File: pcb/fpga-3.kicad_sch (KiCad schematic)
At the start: 6 parts, among them U7 XC7A100T-FGG484, Y1 SiT9365AI-2B2-33E200.000000

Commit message: jtag, dcplng
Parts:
- added C109, C110, C111, C112, C113, C114, C115, C116, C117, C118, C119, C120: 0.1uF, Capacitor_SMD:C_0402_1005Metric, symbol library:C
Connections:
- net 1V35_FD: now also C109.2, C110.2, C111.2, C112.2, C113.2, C114.2, C115.2, C116.2, C117.2, C118.2, C119.2, C120.2
- net GND: now also C109.1, C110.1, C111.1, C112.1, C113.1, C114.1, C115.1, C116.1, C117.1, C118.1, C119.1, C120.1

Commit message: decoupling
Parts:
- removed C109, C110, C111, C112, C113, C114: 0.1uF, Capacitor_SMD:C_0402_1005Metric, symbol library:C
- added C146, C147, C148, C149, C150, C151: 0.1uF, Capacitor_SMD:C_0402_1005Metric, symbol library:C
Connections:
- net GND: now also C146.1, C147.1, C148.1, C149.1, C150.1, C151.1
- net 1V35_FD renamed 1V35_DDR
- net 1V35_DDR: now also C146.2, C147.2, C148.2, C149.2, C150.2, C151.2

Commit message: bom
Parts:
- C42: renamed from C17; Part Description 0.1uF 10% 16V Ceramic Capacitor X7R 0402 (1005 Metric) -> CAP CER 0.1UF 16V X7R 0402
- C43: renamed from C18; Part Description 0.1uF 10% 16V Ceramic Capacitor X7R 0402 (1005 Metric) -> CAP CER 0.1UF 16V X7R 0402
- C44: renamed from C146; Part Description (none) -> CAP CER 0.1UF 16V X7R 0402
- C45: renamed from C115; Part Description (none) -> CAP CER 0.1UF 16V X7R 0402
- C46: renamed from C147; Part Description (none) -> CAP CER 0.1UF 16V X7R 0402
- C47: renamed from C116; Part Description (none) -> CAP CER 0.1UF 16V X7R 0402
- C48: renamed from C148; Part Description (none) -> CAP CER 0.1UF 16V X7R 0402
- C49: renamed from C117; Part Description (none) -> CAP CER 0.1UF 16V X7R 0402
- C50: renamed from C149; Part Description (none) -> CAP CER 0.1UF 16V X7R 0402
- C51: renamed from C118; Part Description (none) -> CAP CER 0.1UF 16V X7R 0402
- C52: renamed from C150; Part Description (none) -> CAP CER 0.1UF 16V X7R 0402
- C53: renamed from C119; Part Description (none) -> CAP CER 0.1UF 16V X7R 0402
- C54: renamed from C151; Part Description (none) -> CAP CER 0.1UF 16V X7R 0402
- C55: renamed from C120; Part Description (none) -> CAP CER 0.1UF 16V X7R 0402
- R23: renamed from R22; Manufacturer (none) -> Vishay Dale; Manufacturer Product Number (none) -> CRCW04024K70FKED; Part Description (none) -> RES 4.7K OHM 1% 1/16W 0402
- R24: renamed from R23; Manufacturer (none) -> Vishay Dale; Manufacturer Product Number (none) -> CRCW04024K70FKED; Part Description (none) -> RES 4.7K OHM 1% 1/16W 0402
- U7: Manufacturer (none) -> AMD; Manufacturer Product Number (none) -> XC7A100T-1FGG484C; Part Description (none) -> IC FPGA 285 I/O 484FBGA
- Y1: Manufacturer (none) -> SiTime; Manufacturer Product Number (none) -> SIT9365AI-2B2-33E200.000000; Part Description (none) -> MEMS OSC XO 200.0000MHZ LVDS SMD

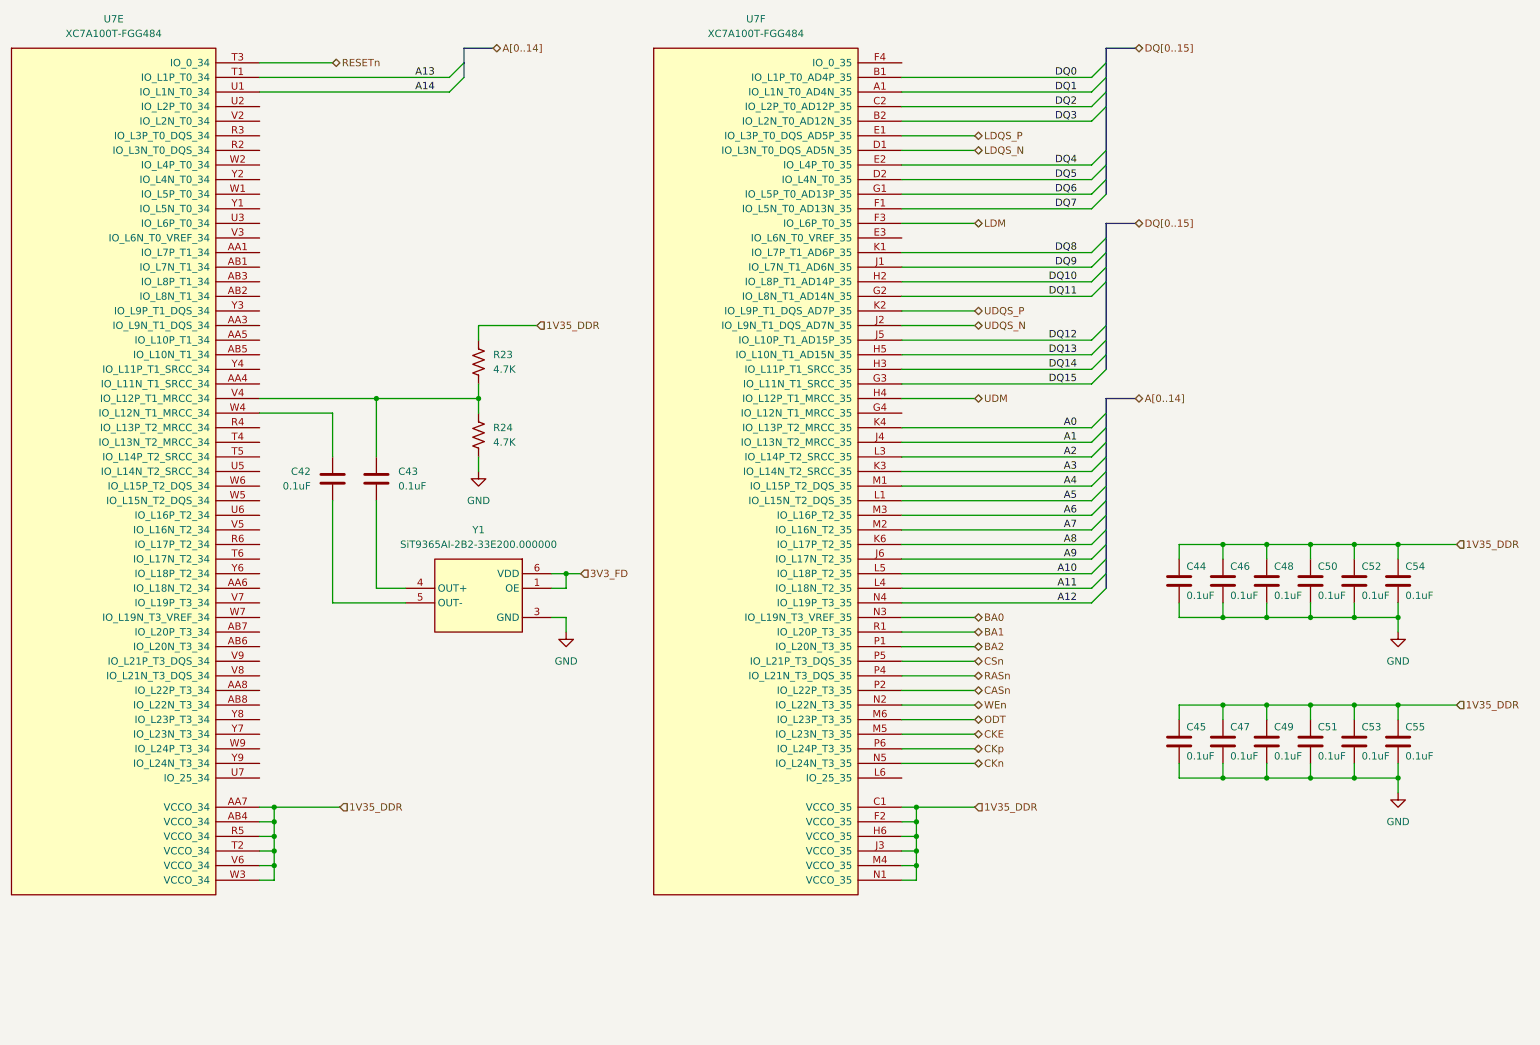
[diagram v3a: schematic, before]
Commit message: added mig ddr pinout constraints
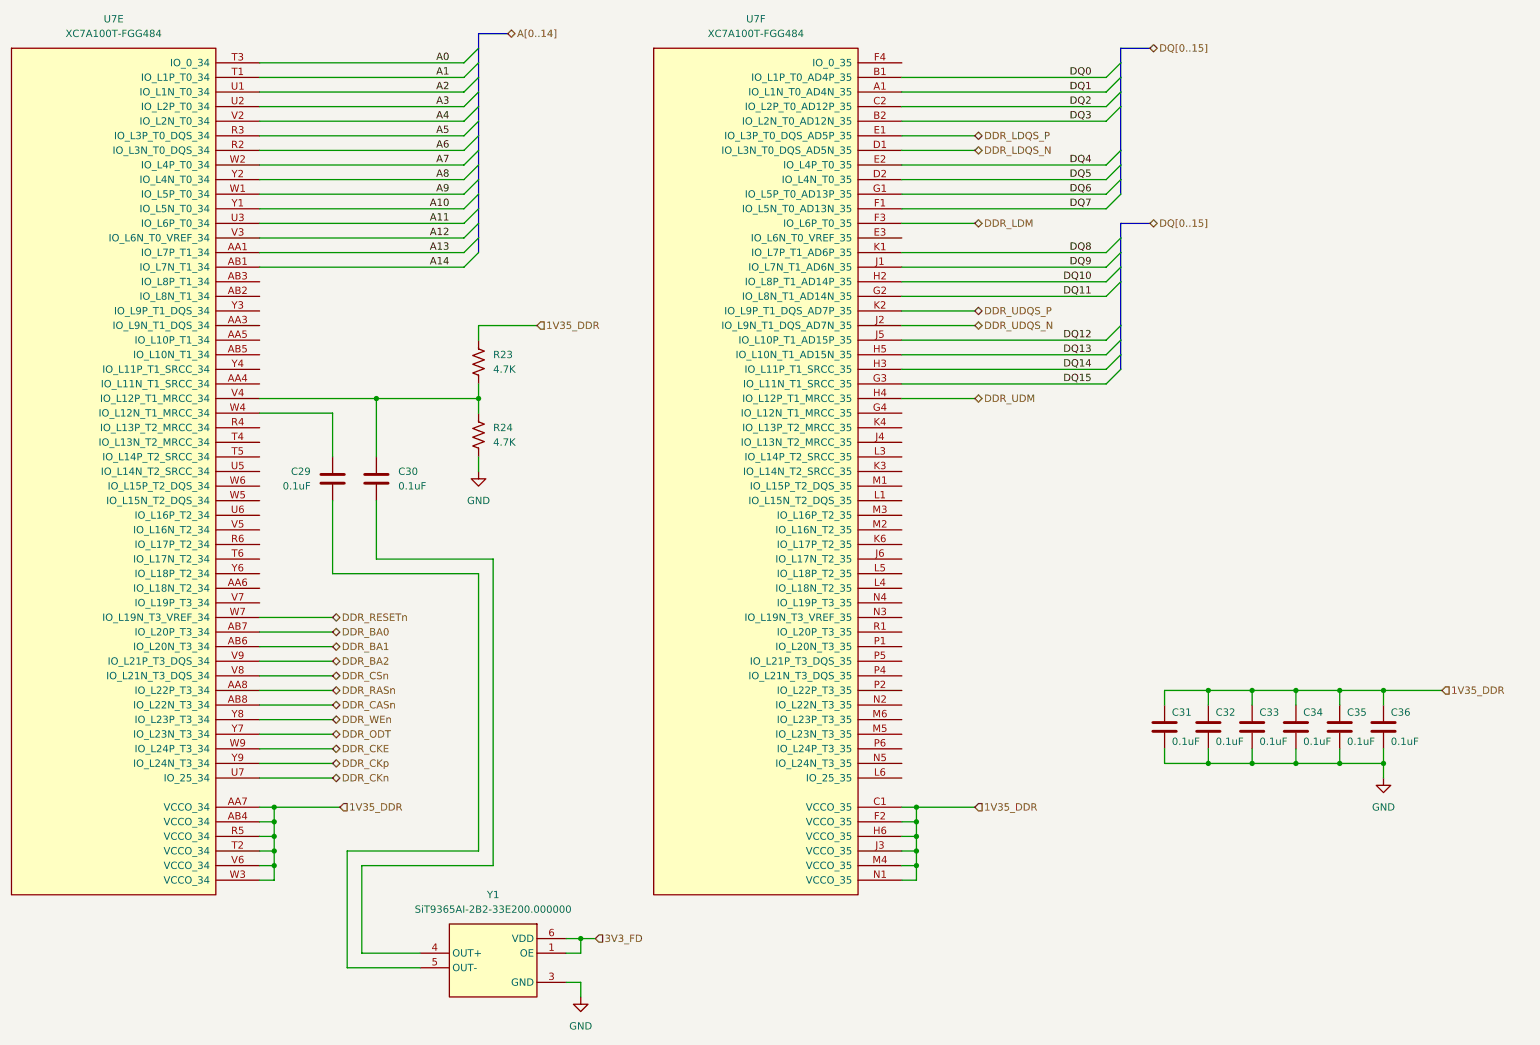
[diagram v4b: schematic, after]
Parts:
- removed C45, C47, C49, C51, C53, C55: 0.1uF, Capacitor_SMD:C_0402_1005Metric, symbol library:C
- renumbered C42 to C29, C43 to C30, C44 to C31, C46 to C32, C48 to C33, C50 to C34, C52 to C35, C54 to C36
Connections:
- net RESETn is gone; now on net A0: U7.T3 (IO_0_34)
- net A0: no longer U7.K4 (IO_L13P_T2_MRCC_35)
- net A1: now also U7.T1 (IO_L1P_T0_34); no longer U7.J4 (IO_L13N_T2_MRCC_35)
- net A10: now also U7.Y1 (IO_L5N_T0_34); no longer U7.L5 (IO_L18P_T2_35)
- net A11: now also U7.U3 (IO_L6P_T0_34); no longer U7.L4 (IO_L18N_T2_35)
- net A12: now also U7.V3 (IO_L6N_T0_VREF_34); no longer U7.N4 (IO_L19P_T3_35)
- net A13: now also U7.AA1 (IO_L7P_T1_34); no longer U7.T1 (IO_L1P_T0_34)
- net A14: now also U7.AB1 (IO_L7N_T1_34); no longer U7.U1 (IO_L1N_T0_34)
- net A2: now also U7.U1 (IO_L1N_T0_34); no longer U7.L3 (IO_L14P_T2_SRCC_35)
- net A3: now also U7.U2 (IO_L2P_T0_34); no longer U7.K3 (IO_L14N_T2_SRCC_35)
- net A4: now also U7.V2 (IO_L2N_T0_34); no longer U7.M1 (IO_L15P_T2_DQS_35)
- net A5: now also U7.R3 (IO_L3P_T0_DQS_34); no longer U7.L1 (IO_L15N_T2_DQS_35)
- net A6: now also U7.R2 (IO_L3N_T0_DQS_34); no longer U7.M3 (IO_L16P_T2_35)
- net A7: now also U7.W2 (IO_L4P_T0_34); no longer U7.M2 (IO_L16N_T2_35)
- net A8: now also U7.Y2 (IO_L4N_T0_34); no longer U7.K6 (IO_L17P_T2_35)
- net A9: now also U7.W1 (IO_L5P_T0_34); no longer U7.J6 (IO_L17N_T2_35)
- net DDR_RASn: now reaches U7.AA8 (IO_L22P_T3_34)
- net DDR_BA1: now reaches U7.AB6 (IO_L20N_T3_34)
- net DDR_BA0: now reaches U7.AB7 (IO_L20P_T3_34)
- net DDR_CASn: now reaches U7.AB8 (IO_L22N_T3_34)
- net DDR_CKn: now reaches U7.U7 (IO_25_34)
- net DDR_CSn: now reaches U7.V8 (IO_L21N_T3_DQS_34)
- net DDR_BA2: now reaches U7.V9 (IO_L21P_T3_DQS_34)
- net DDR_RESETn: now reaches U7.W7 (IO_L19N_T3_VREF_34)
- net DDR_CKE: now reaches U7.W9 (IO_L24P_T3_34)
- net DDR_ODT: now reaches U7.Y7 (IO_L23N_T3_34)
- net DDR_WEn: now reaches U7.Y8 (IO_L23P_T3_34)
- net DDR_CKp: now reaches U7.Y9 (IO_L24N_T3_34)
- net BA0: no longer names the net of U7.N3 (IO_L19N_T3_VREF_35)
- net BA1: no longer names the net of U7.R1 (IO_L20P_T3_35)
- net BA2: no longer names the net of U7.P1 (IO_L20N_T3_35)
- net CASn: no longer names the net of U7.P2 (IO_L22P_T3_35)
- net CKE: no longer names the net of U7.M5 (IO_L23N_T3_35)
- net CKn: no longer names the net of U7.N5 (IO_L24N_T3_35)
- net CKp: no longer names the net of U7.P6 (IO_L24P_T3_35)
- net CSn: no longer names the net of U7.P5 (IO_L21P_T3_DQS_35)
- net LDM renamed DDR_LDM
- net LDQS_N renamed DDR_LDQS_N
- net LDQS_P renamed DDR_LDQS_P
- net ODT: no longer names the net of U7.M6 (IO_L23P_T3_35)
- net RASn: no longer names the net of U7.P4 (IO_L21N_T3_DQS_35)
- net UDM renamed DDR_UDM
- net UDQS_N renamed DDR_UDQS_N
- net UDQS_P renamed DDR_UDQS_P
- net WEn: no longer names the net of U7.N2 (IO_L22N_T3_35)
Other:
- moved on the sheet: C31, C32, C33, C34, C35, C36, Y1

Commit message: real ddr pinout done
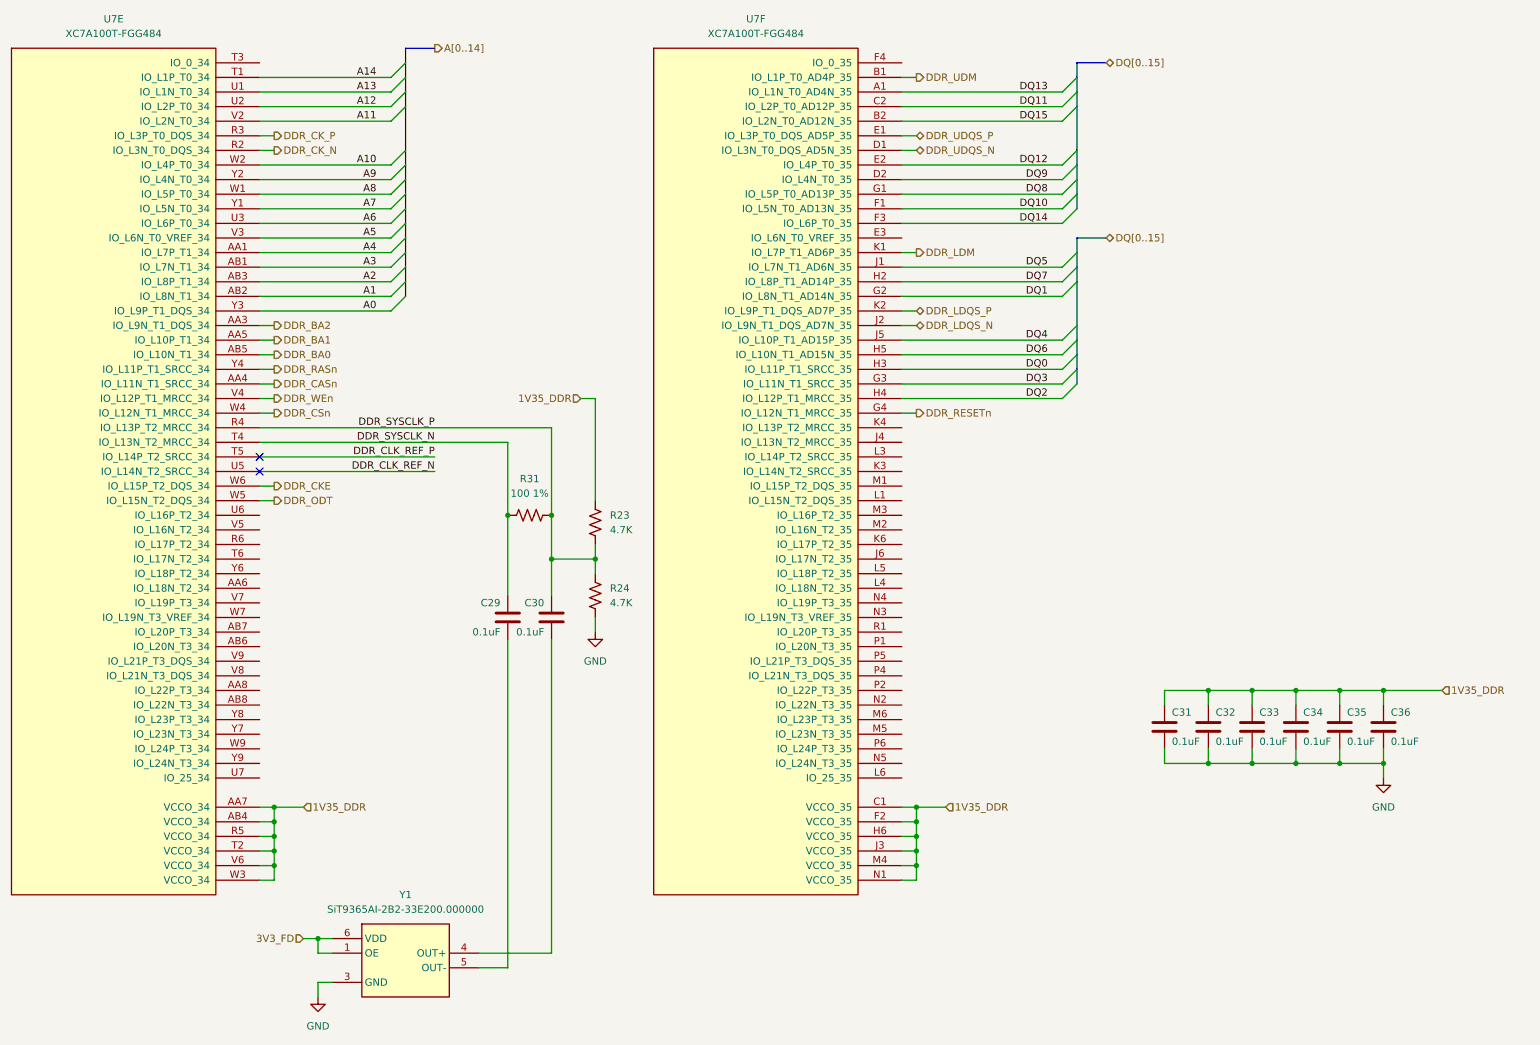
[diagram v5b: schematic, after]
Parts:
- added R31: 100 1%, Resistor_SMD:R_0402_1005Metric, symbol library:R_US
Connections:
- net A0: now also U7.Y3 (IO_L9P_T1_DQS_34); no longer U7.T3 (IO_0_34)
- net A1: now also U7.AB2 (IO_L8N_T1_34); no longer U7.T1 (IO_L1P_T0_34)
- net A10: now also U7.W2 (IO_L4P_T0_34); no longer U7.Y1 (IO_L5N_T0_34)
- net A11: now also U7.V2 (IO_L2N_T0_34); no longer U7.U3 (IO_L6P_T0_34)
- net A12: now also U7.U2 (IO_L2P_T0_34); no longer U7.V3 (IO_L6N_T0_VREF_34)
- net A13: now also U7.U1 (IO_L1N_T0_34); no longer U7.AA1 (IO_L7P_T1_34)
- net A14: now also U7.T1 (IO_L1P_T0_34); no longer U7.AB1 (IO_L7N_T1_34)
- net A2: now also U7.AB3 (IO_L8P_T1_34); no longer U7.U1 (IO_L1N_T0_34)
- net A3: now also U7.AB1 (IO_L7N_T1_34); no longer U7.U2 (IO_L2P_T0_34)
- net A4: now also U7.AA1 (IO_L7P_T1_34); no longer U7.V2 (IO_L2N_T0_34)
- net A5: now also U7.V3 (IO_L6N_T0_VREF_34); no longer U7.R3 (IO_L3P_T0_DQS_34)
- net A6: now also U7.U3 (IO_L6P_T0_34); no longer U7.R2 (IO_L3N_T0_DQS_34)
- net A7: now also U7.Y1 (IO_L5N_T0_34); no longer U7.W2 (IO_L4P_T0_34)
- net A8: now also U7.W1 (IO_L5P_T0_34); no longer U7.Y2 (IO_L4N_T0_34)
- net A9: now also U7.Y2 (IO_L4N_T0_34); no longer U7.W1 (IO_L5P_T0_34)
- net DDR_BA0: now also U7.AB5 (IO_L10N_T1_34); no longer U7.AB7 (IO_L20P_T3_34)
- net DDR_BA1: now also U7.AA5 (IO_L10P_T1_34); no longer U7.AB6 (IO_L20N_T3_34)
- net DDR_BA2: now also U7.AA3 (IO_L9N_T1_DQS_34); no longer U7.V9 (IO_L21P_T3_DQS_34)
- net DDR_CASn: now also U7.AA4 (IO_L11N_T1_SRCC_34); no longer U7.AB8 (IO_L22N_T3_34)
- net DDR_CKE: now also U7.W6 (IO_L15P_T2_DQS_34); no longer U7.W9 (IO_L24P_T3_34)
- net DDR_CSn: now also U7.W4 (IO_L12N_T1_MRCC_34); no longer U7.V8 (IO_L21N_T3_DQS_34)
- net DDR_LDM: now also U7.K1 (IO_L7P_T1_AD6P_35); no longer U7.F3 (IO_L6P_T0_35)
- net DDR_LDQS_N: now also U7.J2 (IO_L9N_T1_DQS_AD7N_35); no longer U7.D1 (IO_L3N_T0_DQS_AD5N_35)
- net DDR_LDQS_P: now also U7.K2 (IO_L9P_T1_DQS_AD7P_35); no longer U7.E1 (IO_L3P_T0_DQS_AD5P_35)
- net DDR_ODT: now also U7.W5 (IO_L15N_T2_DQS_34); no longer U7.Y7 (IO_L23N_T3_34)
- net DDR_RASn: now also U7.Y4 (IO_L11P_T1_SRCC_34); no longer U7.AA8 (IO_L22P_T3_34)
- net DDR_RESETn: now also U7.G4 (IO_L12N_T1_MRCC_35); no longer U7.W7 (IO_L19N_T3_VREF_34)
- net DDR_UDM: now also U7.B1 (IO_L1P_T0_AD4P_35); no longer U7.H4 (IO_L12P_T1_MRCC_35)
- net DDR_UDQS_N: now also U7.D1 (IO_L3N_T0_DQS_AD5N_35); no longer U7.J2 (IO_L9N_T1_DQS_AD7N_35)
- net DDR_UDQS_P: now also U7.E1 (IO_L3P_T0_DQS_AD5P_35); no longer U7.K2 (IO_L9P_T1_DQS_AD7P_35)
- net DDR_WEn: now also U7.V4 (IO_L12P_T1_MRCC_34); no longer U7.Y8 (IO_L23P_T3_34)
- net DQ0: now also U7.H3 (IO_L11P_T1_SRCC_35); no longer U7.B1 (IO_L1P_T0_AD4P_35)
- net DQ1: now also U7.G2 (IO_L8N_T1_AD14N_35); no longer U7.A1 (IO_L1N_T0_AD4N_35)
- net DQ10: now also U7.F1 (IO_L5N_T0_AD13N_35); no longer U7.H2 (IO_L8P_T1_AD14P_35)
- net DQ11: now also U7.C2 (IO_L2P_T0_AD12P_35); no longer U7.G2 (IO_L8N_T1_AD14N_35)
- net DQ12: now also U7.E2 (IO_L4P_T0_35); no longer U7.J5 (IO_L10P_T1_AD15P_35)
- net DQ13: now also U7.A1 (IO_L1N_T0_AD4N_35); no longer U7.H5 (IO_L10N_T1_AD15N_35)
- net DQ14: now also U7.F3 (IO_L6P_T0_35); no longer U7.H3 (IO_L11P_T1_SRCC_35)
- net DQ15: now also U7.B2 (IO_L2N_T0_AD12N_35); no longer U7.G3 (IO_L11N_T1_SRCC_35)
- net DQ2: now also U7.H4 (IO_L12P_T1_MRCC_35); no longer U7.C2 (IO_L2P_T0_AD12P_35)
- net DQ3: now also U7.G3 (IO_L11N_T1_SRCC_35); no longer U7.B2 (IO_L2N_T0_AD12N_35)
- net DQ4: now also U7.J5 (IO_L10P_T1_AD15P_35); no longer U7.E2 (IO_L4P_T0_35)
- net DQ5: now also U7.J1 (IO_L7N_T1_AD6N_35); no longer U7.D2 (IO_L4N_T0_35)
- net DQ6: now also U7.H5 (IO_L10N_T1_AD15N_35); no longer U7.G1 (IO_L5P_T0_AD13P_35)
- net DQ7: now also U7.H2 (IO_L8P_T1_AD14P_35); no longer U7.F1 (IO_L5N_T0_AD13N_35)
- net DQ8: now also U7.G1 (IO_L5P_T0_AD13P_35); no longer U7.K1 (IO_L7P_T1_AD6P_35)
- net DQ9: now also U7.D2 (IO_L4N_T0_35); no longer U7.J1 (IO_L7N_T1_AD6N_35)
- net DDR_SYSCLK_P: now reaches U7.R4 (IO_L13P_T2_MRCC_34)
- net DDR_SYSCLK_P: now also C30.1, R23.2, R24.1, R31.2
- net DDR_SYSCLK_N: now reaches U7.T4 (IO_L13N_T2_MRCC_34)
- net DDR_SYSCLK_N: now also C29.1, R31.1
- net DDR_CLK_REF_P: now reaches U7.T5 (IO_L14P_T2_SRCC_34)
- net DDR_CLK_REF_N: now reaches U7.U5 (IO_L14N_T2_SRCC_34)
- net DDR_CKn: no longer names the net of U7.U7 (IO_25_34)
- net DDR_CKp: no longer names the net of U7.Y9 (IO_L24N_T3_34)
- new net DDR_CK_N: U7.R2 (IO_L3N_T0_DQS_34)
- new net DDR_CK_P: U7.R3 (IO_L3P_T0_DQS_34)
- no-connect marks 0 -> 2
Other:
- moved on the sheet: C29, C30, R23, R24, Y1
